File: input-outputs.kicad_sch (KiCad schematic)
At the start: 5 parts, among them J5 I2C-STEMMA-QT, J7 swd, J9 UART

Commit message: LTDC route almost finished
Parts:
- J9: footprint S4B-XH-SM4-TB_LF__SN:S4BXHSM4TBLFSN -> Connector_Hirose:Hirose_DF13C_CL535-0404-8-51_1x04-1MP_P1.25mm_Vertical
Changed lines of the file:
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@@
 			)
 		)
-		(property "Footprint" "S4B-XH-SM4-TB_LF__SN:S4BXHSM4TBLFSN"
+		(property "Footprint" "Connector_Hirose:Hirose_DF13C_CL535-0404-8-51_1x04-1MP_P1.25mm_Vertical"
 			(at 90.17 74.93 0)
 			(effects

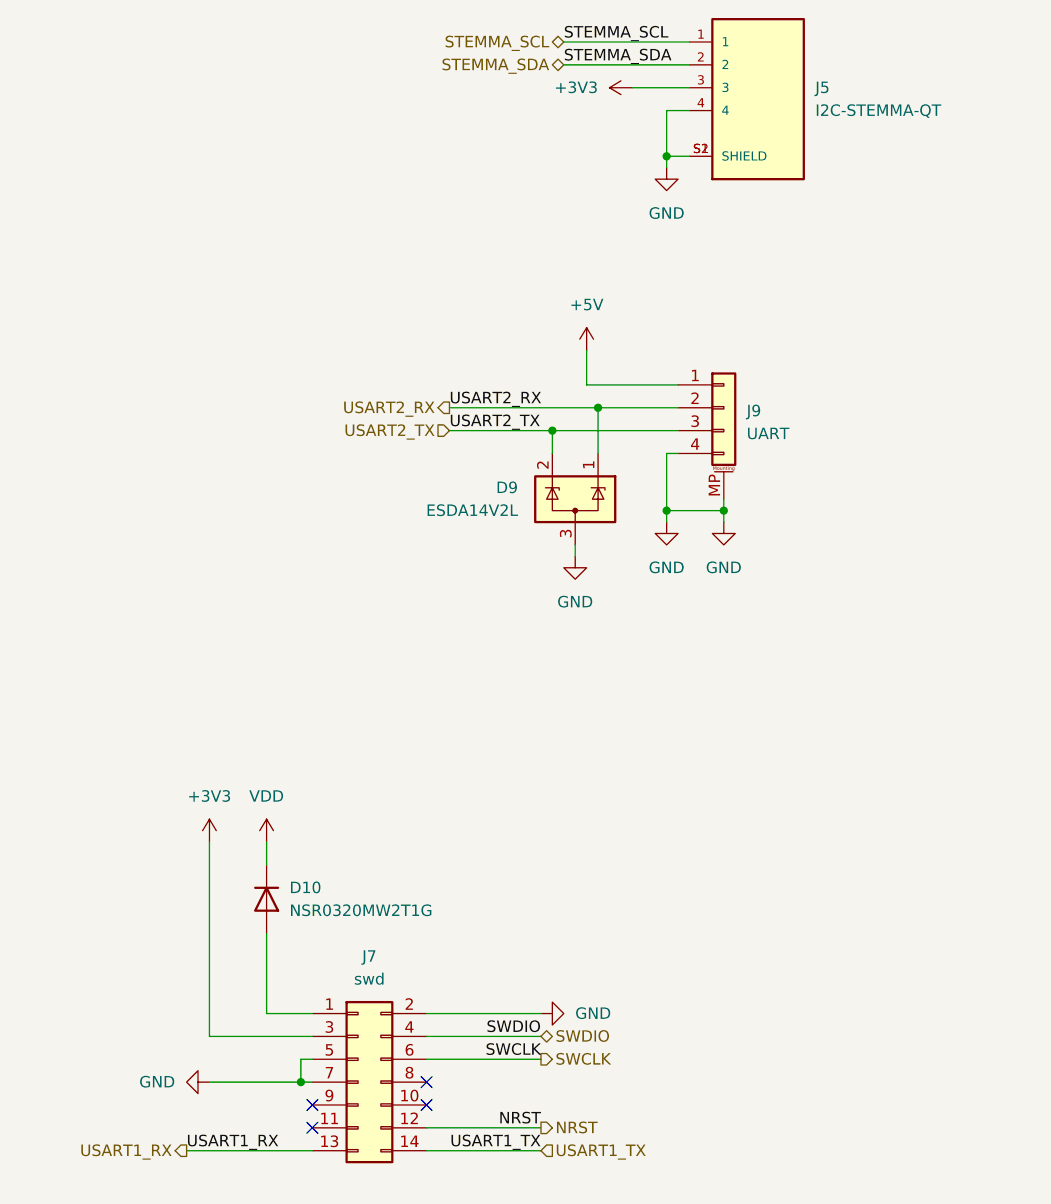
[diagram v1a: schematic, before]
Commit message: Added chroma pixel png
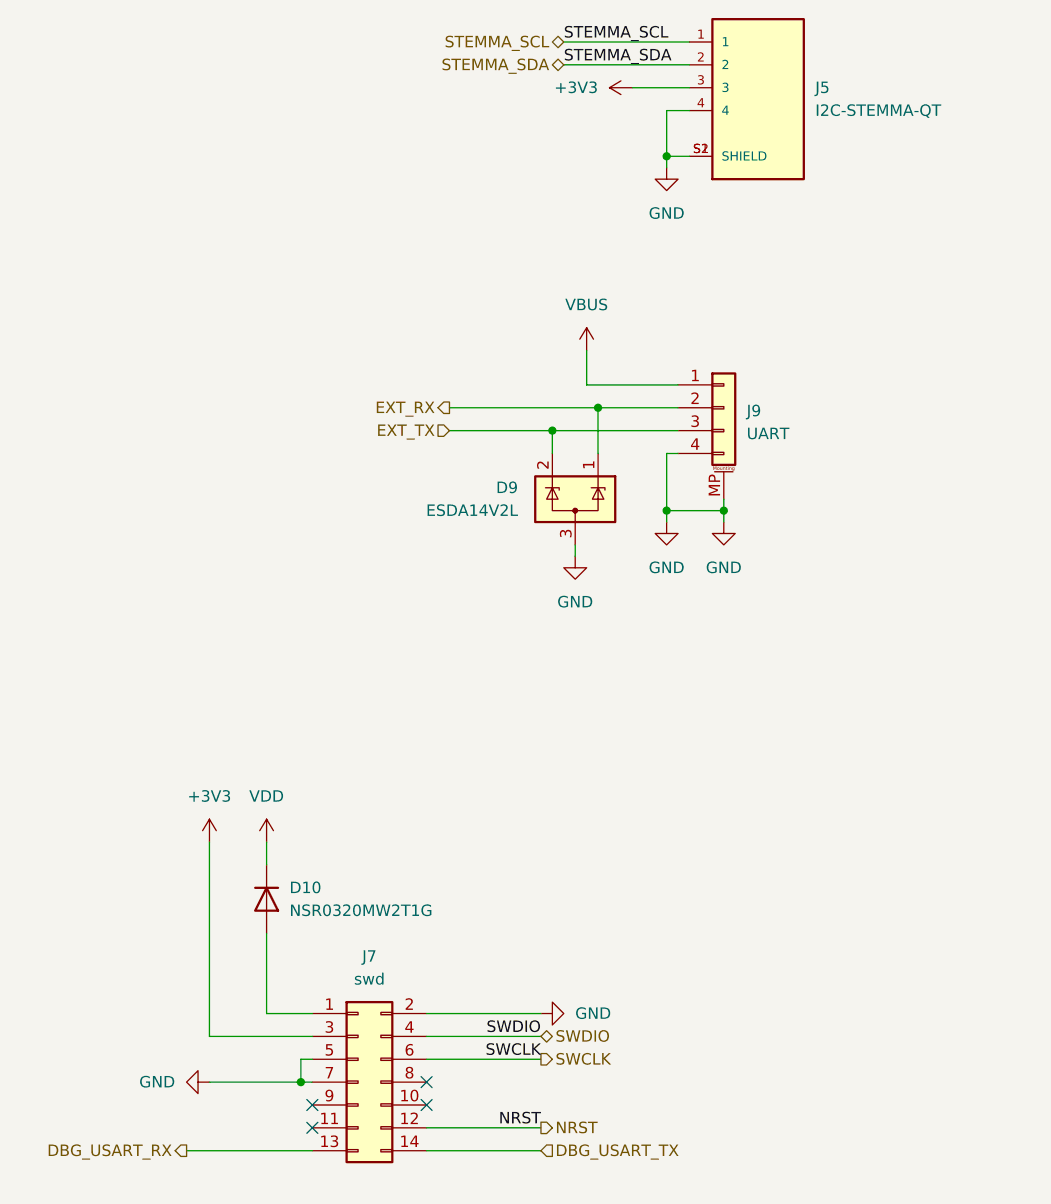
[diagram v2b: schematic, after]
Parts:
- D10: JLCPCB Part # (none) -> C48192
- D9: JLCPCB Part # (none) -> C2682282
- J7: JLCPCB Part # (none) -> C2881912
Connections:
- net +5V renamed VBUS
- net USART1_RX renamed DBG_USART_RX
- net USART1_TX renamed DBG_USART_TX
- net USART2_RX renamed EXT_RX
- net USART2_TX renamed EXT_TX
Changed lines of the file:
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@@
 		)
 	)
-	(label "USART2_TX"
-		(at 59.69 77.47 0)
+	(label "SWDIO"
+		(at 69.85 144.78 180)
 		(fields_autoplaced yes)
 		(effects
@@
 				(size 1.27 1.27)
 			)
-			(justify left bottom)
-		)
-	)
-	(label "USART2_RX"
-		(at 59.69 74.93 0)
+			(justify right bottom)
+		)
+	)
+	(label "NRST"
+		(at 69.85 154.94 180)
 		(fields_autoplaced yes)
 		(effects
@@
 				(size 1.27 1.27)
 			)
-			(justify left bottom)
-		)
-	)
-	(label "SWDIO"
-		(at 69.85 144.78 180)
+			(justify right bottom)
+		)
+	)
+	(label "STEMMA_SDA"
+		(at 72.39 36.83 0)
 		(fields_autoplaced yes)
 		(effects
@@
 				(size 1.27 1.27)
 			)
-			(justify right bottom)
-		)
-	)
-	(label "NRST"
-		(at 69.85 154.94 180)
+			(justify left bottom)
+		)
+	)
+	(hierarchical_label "EXT_TX"
+		(shape input)
+		(at 59.69 77.47 180)
 		(fields_autoplaced yes)
 		(effects
@@
 				(size 1.27 1.27)
 			)
-			(justify right bottom)
-		)
-	)
-	(label "STEMMA_SDA"
-		(at 72.39 36.83 0)
+			(justify right)
+		)
+	)
+	(hierarchical_label "STEMMA_SCL"
+		(shape bidirectional)
+		(at 72.39 34.29 180)
 		(fields_autoplaced yes)
 		(effects
@@
 				(size 1.27 1.27)
 			)
-			(justify left bottom)
-		)
-	)
-	(label "USART1_RX"
-		(at 30.48 157.48 0)
+			(justify right)
+		)
+	)
+	(hierarchical_label "SWDIO"
+		(shape bidirectional)
+		(at 69.85 144.78 0)
 		(fields_autoplaced yes)
 		(effects
@@
 				(size 1.27 1.27)
 			)
-			(justify left bottom)
-		)
-	)
-	(label "USART1_TX"
-		(at 69.85 157.48 180)
+			(justify left)
+		)
+	)
+	(hierarchical_label "DBG_USART_RX"
+		(shape output)
+		(at 30.48 157.48 180)
 		(fields_autoplaced yes)
 		(effects
@@
 				(size 1.27 1.27)
 			)
-			(justify right bottom)
-		)
-	)
-	(hierarchical_label "USART2_TX"
-		(shape input)
-		(at 59.69 77.47 180)
+			(justify right)
+		)
+	)
+	(hierarchical_label "SWCLK"
+		(shape output)
+		(at 69.85 147.32 0)
 		(fields_autoplaced yes)
 		(effects
@@
 				(size 1.27 1.27)
 			)
-			(justify right)
-		)
-	)
-	(hierarchical_label "STEMMA_SCL"
-		(shape bidirectional)
-		(at 72.39 34.29 180)
+			(justify left)
+		)
+	)
+	(hierarchical_label "DBG_USART_TX"
+		(shape input)
+		(at 69.85 157.48 0)
 		(fields_autoplaced yes)
 		(effects
@@
 				(size 1.27 1.27)
 			)
-			(justify right)
-		)
-	)
-	(hierarchical_label "SWDIO"
-		(shape bidirectional)
-		(at 69.85 144.78 0)
-		(fields_autoplaced yes)
-		(effects
-			(font
-				(size 1.27 1.27)
-			)
 			(justify left)
 		)
 	)
-	(hierarchical_label "USART1_RX"
-		(shape output)
-		(at 30.48 157.48 180)
-		(fields_autoplaced yes)
-		(effects
-			(font
-				(size 1.27 1.27)
-			)
-			(justify right)
-		)
-	)
-	(hierarchical_label "SWCLK"
-		(shape output)
-		(at 69.85 147.32 0)
-		(fields_autoplaced yes)
-		(effects
-			(font
-				(size 1.27 1.27)
-			)
-			(justify left)
-		)
-	)
-	(hierarchical_label "USART1_TX"
-		(shape input)
-		(at 69.85 157.48 0)
-		(fields_autoplaced yes)
-		(effects
-			(font
-				(size 1.27 1.27)
-			)
-			(justify left)
-		)
-	)
-	(hierarchical_label "USART2_RX"
+	(hierarchical_label "EXT_RX"
 		(shape output)
 		(at 59.69 74.93 180)
@@
 			)
 		)
+		(property "JLCPCB Part #" "C2881912"
+			(at 49.53 149.86 0)
+			(effects
+				(font
+					(size 1.27 1.27)
+				)
+				(hide yes)
+			)
+		)
 		(pin "6"
 		)
@@
 		)
 		(property "Sim.Pins" "1=K 2=A"
+			(at 39.37 129.54 0)
+			(effects
+				(font
+					(size 1.27 1.27)
+				)
+				(hide yes)
+			)
+		)
+		(property "JLCPCB Part #" "C48192"
 			(at 39.37 129.54 0)
 			(effects
@@
 			)
 		)
+		(property "JLCPCB Part #" "C2682282"
+			(at 73.66 85.09 0)
+			(effects
+				(font
+					(size 1.27 1.27)
+				)
+				(hide yes)
+			)
+		)
 		(pin "3"
 		)
@@
 	)
 	(symbol
-		(lib_id "power:+5V")
+		(lib_id "power:VBUS")
 		(at 74.93 68.58 0)
 		(unit 1)
@@
 		(dnp no)
 		(fields_autoplaced yes)
-		(property "Reference" "#PWR0106"
+		(property "Reference" "#PWR07"
 			(at 74.93 72.39 0)
 			(effects
@@
 			)
 		)
-		(property "Value" "+5V"
+		(property "Value" "VBUS"
 			(at 74.93 63.5 0)
 			(effects
@@
 			)
 		)
-		(property "Description" "Power symbol creates a global label with name \"+5V\""
+		(property "Description" "Power symbol creates a global label with name \"VBUS\""
 			(at 74.93 68.58 0)
 			(effects
@@
 			(project "chroma-pixel-h743"
 				(path "/70094798-b7e4-48a4-a512-b8f48be18f9f/cf3c6c38-1b0f-4722-9440-d8d8f6f0e2e1"
-					(reference "#PWR0106")
+					(reference "#PWR07")
 					(unit 1)
 				)

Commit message: First release H743 version
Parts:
- J9: JLCPCB Part # C146120 -> C7430470
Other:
- note added: "This pin connected to MCU USART RX"
- note added: "This pin connected to MCU USART TX"
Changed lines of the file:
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@@
+		)
+	)
+	(text "This pin connected to MCU USART RX"
+		(exclude_from_sim no)
+		(at 33.02 160.274 0)
+		(effects
+			(font
+				(size 1.27 1.27)
+			)
+		)
+	)
+	(text "This pin connected to MCU USART TX"
+		(exclude_from_sim no)
+		(at 103.378 157.734 0)
+		(effects
+			(font
+				(size 1.27 1.27)
+			)
 		)
 	)
@@
 			)
 		)
-		(property "JLCPCB Part #" "C146120"
+		(property "JLCPCB Part #" "C7430470"
 			(at 90.17 74.93 0)
 			(effects
